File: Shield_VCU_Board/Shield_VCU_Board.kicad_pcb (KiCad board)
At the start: 2 copper layers, 250.5 x 107.1 mm, 148 parts, among them J1 Conn_02x08_Odd_Even, J10 Main_Supply, J11 Conn_01x40_Socket, J13 Conn_Molex_TouchPanel, J14 CAN_OUT, J15 Conn_01x04_Socket, J2 Conn_02x10_Odd_Even, J3/1 NXP3, J4 Conn_02x08_Odd_Even, J5 Conn_02x10_Odd_Even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

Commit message: 7seg+LED changes
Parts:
- added Q1: BFR92, Package_TO_SOT_SMD:SOT-323_SC-70, B.Cu at (258.2, 62.8)
- added Q2: BFR92, Package_TO_SOT_SMD:SOT-323_SC-70, B.Cu at (258.2, 73.8)
- added Q3: BFR92, Package_TO_SOT_SMD:SOT-323_SC-70, B.Cu at (258.2, 84.7)
- added Q4: BFR92, Package_TO_SOT_SMD:SOT-323_SC-70, B.Cu at (258.2, 95.8)
- added R1: 1k, Resistor_SMD:R_1206_3216Metric_Pad1.30x1.75mm_HandSolder, B.Cu at (257.6, 59.3)
- added R17: 1k, Resistor_SMD:R_1206_3216Metric_Pad1.30x1.75mm_HandSolder, B.Cu at (257.6, 69.9)
- added R18: 1k, Resistor_SMD:R_1206_3216Metric_Pad1.30x1.75mm_HandSolder, B.Cu at (257.6, 80.6)
- added R23: 1k, Resistor_SMD:R_1206_3216Metric_Pad1.30x1.75mm_HandSolder, B.Cu at (257.6, 91.2)
- moved C36 30.1 mm to (107.3, 84.8), turned to 180 degrees
- moved PD1 4.46 mm to (163.5, 75.2)
- moved R20 2.64 mm to (178.4, 72.1)
- moved INT1 2.56 mm to (162.6, 72.1)
- moved CS1 2.42 mm to (162.3, 68.9)
- moved R21 2.24 mm to (178.3, 74.4)
- moved MOSI1 1.10 mm to (153.7, 66.0)
- moved MISO1 0.71 mm to (151.5, 65.0)
- moved SCK1 0.30 mm to (149.3, 63.7)
- turned C35 to 90 degrees
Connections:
- net Net-(U1-DIG0) renamed /7U8
- net Net-(U1-DIG1) renamed /7U5
- net Net-(U1-DIG2) renamed /7U2
- net Net-(U1-DIG3) renamed /7U7
- net Net-(U1-DIG4) renamed /7U1
- net Net-(U1-DIG5) renamed /7U4
- net Net-(U1-DIG6) renamed /7U6
- net Net-(U1-DIG7) renamed /7U3
- J2 pad 1: MC_INT -> MC_PD
- J2 pad 15: unconnected-(J2-Pin_15-Pad15) -> AUD_SHDN
- J2 pad 2: AUD_SHDN -> unconnected-(J2-Pin_2-Pad2)
- J2 pad 3: MC_PD -> MC_INT
- R2 pad 1: LED1_PTB9 -> Net-(Q1-E)
- R3 pad 1: LED2_PTA12 -> Net-(Q2-E)
- R4 pad 1: LED3_PTA24 -> Net-(Q3-E)
- R5 pad 1: LED4_PTA25 -> Net-(Q4-E)
- U3 pad 10: FT_PD -> FT_INT
- U3 pad 11: MC_PD -> MC_INT
- U3 pad 8: MC_INT -> MC_PD
- U3 pad 9: FT_INT -> FT_PD
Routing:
- net +12V: track 343.1 -> 500.2 mm
- net LED4_PTA25: track 2.40 -> 34.9 mm
- net LED3_PTA24: track 2.88 -> 24.9 mm
- net LED1_PTB9: track 3.06 -> 20.5 mm
- net LED2_PTA12: track 2.49 -> 19.9 mm
- net AUD_SHDN: track 107.2 -> 94.2 mm
- net FT_INT: track 84.8 -> 79.3 mm, vias 2 -> 0
- net Net-(Q4-E): track 0.00 -> 5.00 mm
- net Net-(Q2-E): track 0.00 -> 4.89 mm
- net Net-(Q3-E): track 0.00 -> 4.77 mm
- net Net-(Q1-E): track 0.00 -> 4.77 mm
- net Net-(Q4-B): track 0.00 -> 3.90 mm
- net Net-(Q3-B): track 0.00 -> 3.43 mm
- net FT_PD: track 75.8 -> 79.2 mm
- net 3V3_DSPL: track 191.9 -> 188.5 mm
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
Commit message: All_wires_to_0.2mm
All the wires had the size forced to 0.2mm
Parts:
- removed F1: Fuse_3A, Fuse:Fuseholder_Blade_Mini_Keystone_3568
- RN8: value R_Pack_33R_04 -> 33R
- moved J10 18.4 mm to (48.0, 56.7), turned to 90 degrees
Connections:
- J10 pad 2: Net-(J10-Pin_2) -> +12V
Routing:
- net GND: track 277.1 -> 437.3 mm, vias 21 -> 26
- net LED4_PTA25: track 34.9 -> 76.9 mm
- net LED3_PTA24: track 24.9 -> 66.9 mm
- net LED2_PTA12: track 19.9 -> 61.9 mm
- net LED1_PTB9: track 20.5 -> 62.5 mm
- net Net-(J10-Pin_2): track 26.1 -> 0.00 mm
- net AUD_SHDN: track 94.2 -> 90.7 mm
- net Net-(7U1-G): track 156.6 -> 158.5 mm
- net Net-(7U1-B): track 165.0 -> 166.6 mm
- net Net-(7U1-F): track 159.1 -> 160.5 mm
- net 7S_NXP_SCL: track 235.3 -> 234.5 mm
- net 5V_BKLT: track 33.2 -> 32.6 mm
- net LED_A: track 19.8 -> 19.2 mm

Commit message: Wires sized
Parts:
- added NT1: NetTie_2, NetTie:NetTie-2_SMD_Pad2.0mm, F.Cu at (140.9, 47.7)
- moved C10 1.66 mm to (81.0, 76.6)
- moved C11 1.66 mm to (83.2, 76.6)
- moved C9 1.66 mm to (78.8, 76.6)
- moved AUDV3.3 0.61 mm to (77.4, 92.1)
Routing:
- net GND: track 437.3 -> 447.7 mm, vias 26 -> 27
- net Net-(RN8-R3.2): track 55.5 -> 60.1 mm
- net 3V3_DSPL: track 188.5 -> 186.2 mm
- net Net-(RN8-R4.2): track 53.0 -> 54.3 mm
- net 3V3_SPKR: track 37.0 -> 38.4 mm
- net Net-(C3-Pad1): track 5.52 -> 6.64 mm
- net GNDA: track 53.3 -> 54.2 mm
- net 5V_BKLT: track 32.6 -> 31.7 mm
- net Net-(D14-A): track 3.51 -> 4.22 mm
- net BL_PWM: track 54.8 -> 55.4 mm
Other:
- board text added: "1.Change wires width depending on current consumption 2.Connect all required vias for GND planes"

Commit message: LED supply wires correction
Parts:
- moved R17 1.10 mm to (256.6, 70.5)
- moved R1 1.02 mm to (256.6, 59.7)
- moved R18 1.01 mm to (256.6, 80.2)
- moved R23 0.98 mm to (256.6, 91.5)
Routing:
- net +12V: track 500.5 -> 457.3 mm
- net GND: track 447.7 -> 460.0 mm
- net LED1_PTB9: track 62.5 -> 54.3 mm, vias 1 -> 0
- net LED2_PTA12: track 61.9 -> 54.8 mm, vias 1 -> 0
- net LED4_PTA25: track 76.9 -> 71.7 mm, vias 1 -> 0
- net LED3_PTA24: track 66.9 -> 62.2 mm, vias 1 -> 0
- net Net-(J2-Pin_12): track 1.54 -> 0.39 mm
- net /7U2: track 60.8 -> 61.6 mm
- net Net-(Q3-B): track 3.43 -> 4.20 mm
- net Net-(7U1-A): track 166.0 -> 165.4 mm
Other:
- board text removed: "1.Change wires width depending on current consumption 2.Connect all required vias for GND planes"

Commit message: GND empty spot extension
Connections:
- J2 pad 10: LED1_PTB9 -> unconnected-(J2-Pin_10-Pad10)
- J2 pad 4: LED2_PTA12 -> unconnected-(J2-Pin_4-Pad4)
- J2 pad 6: LED3_PTA24 -> unconnected-(J2-Pin_6-Pad6)
- J2 pad 8: LED4_PTA25 -> unconnected-(J2-Pin_8-Pad8)
- J6 pad 11: unconnected-(J6-Pin_11-Pad11) -> LED3_PTA24
- J6 pad 13: unconnected-(J6-Pin_13-Pad13) -> LED4_PTA25
- J6 pad 7: unconnected-(J6-Pin_7-Pad7) -> LED1_PTB9
- J6 pad 9: unconnected-(J6-Pin_9-Pad9) -> LED2_PTA12
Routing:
- net LED1_PTB9: track 54.3 -> 31.9 mm
- net LED2_PTA12: track 54.8 -> 35.4 mm
- net LED3_PTA24: track 62.2 -> 45.7 mm
- net LED4_PTA25: track 71.7 -> 58.1 mm
- net +12V: track 457.3 -> 457.9 mm
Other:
- board text removed: "!!!GND planes NOT connected!!!"

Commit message: GND lines added + JST connector
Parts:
- J7: footprint Connector_PinSocket_2.00mm:PinSocket_2x01_P2.00mm_Vertical_SMD -> ALibrary:JST_PH_B2B-PH-K_1x02_P2.00mm_Vertical_GHST
- J8: footprint Connector_Molex:Molex_KK-396_A-41791-0002_1x02_P3.96mm_Vertical -> ALibrary:JST_PH_B2B-PH-K_1x02_P2.00mm_Vertical_GHST
- moved SCK1 14.2 mm to (163.5, 64.6)
- moved MISO1 12.1 mm to (163.5, 66.8)
- moved MOSI1 10.2 mm to (163.5, 68.9)
- moved J8 2.75 mm to (78.2, 70.7)
- moved CS1 2.49 mm to (163.5, 71.1)
- moved INT1 1.45 mm to (163.5, 73.2)
- moved NT1 0.90 mm to (140.9, 48.6)
- moved PD1 0.20 mm to (163.5, 75.4)
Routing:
- net GND: track 460.0 -> 808.7 mm, vias 27 -> 47
- net Net-(7U1-G): track 158.5 -> 167.3 mm
- net Net-(J8-Pin_1): track 14.0 -> 11.3 mm
- net FT_MOSI: track 84.2 -> 86.6 mm
- net Net-(RN8-R3.2): track 60.1 -> 57.9 mm
- net /7U3: track 47.1 -> 44.9 mm
- net 3V3_DSPL: track 186.2 -> 188.3 mm
- net FT_T_SCK: track 83.9 -> 86.0 mm
- net FT_MISO: track 83.1 -> 85.0 mm
- net Net-(J8-Pin_2): track 20.7 -> 18.8 mm
- net /7U6: track 26.0 -> 24.2 mm
- net Net-(7U1-A): track 165.4 -> 163.7 mm
- net /7U2: track 61.6 -> 60.8 mm
- net FT_CS: track 81.0 -> 81.6 mm
- net FT_INT: track 79.3 -> 79.8 mm

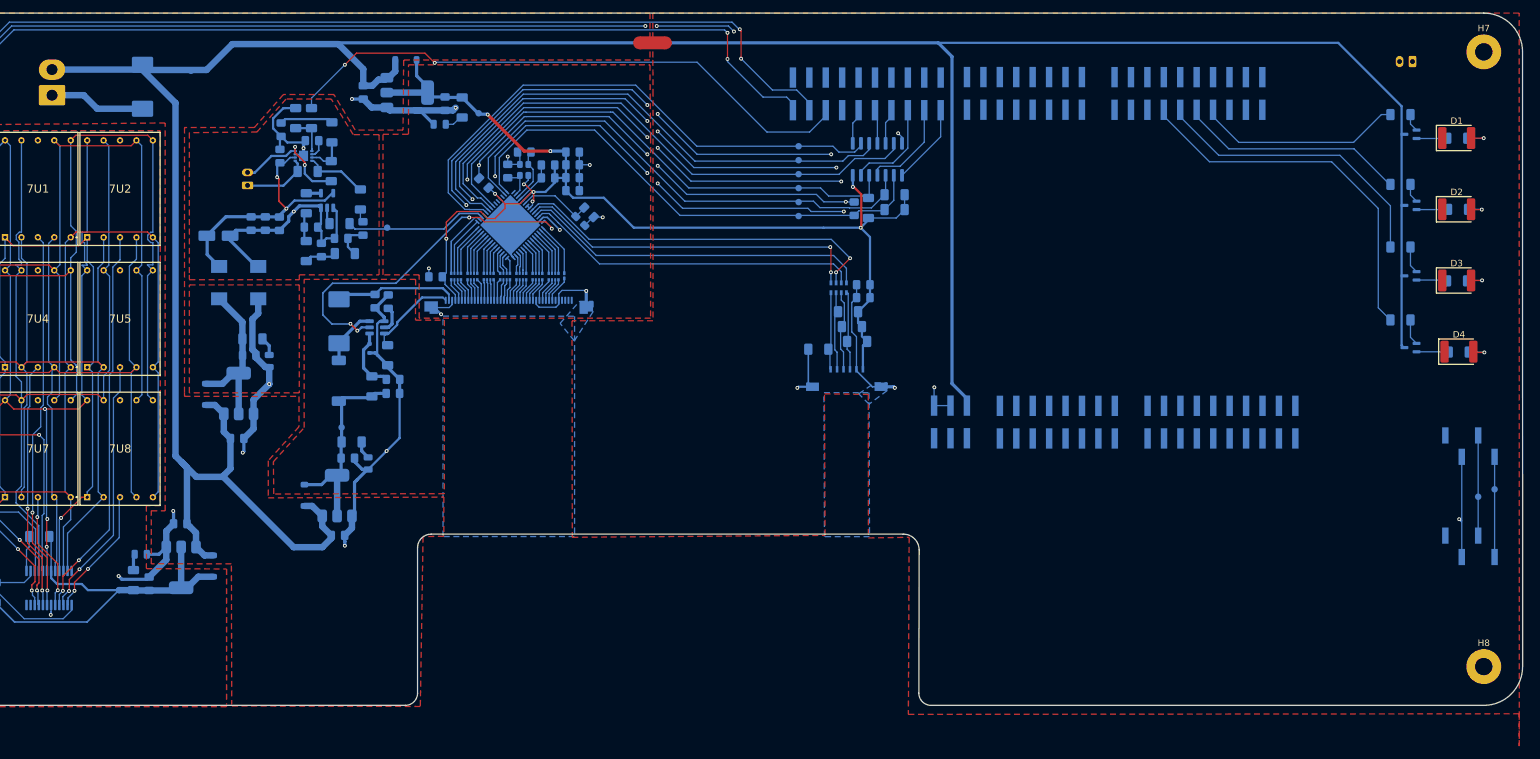
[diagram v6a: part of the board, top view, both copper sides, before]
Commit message: JST connectors added
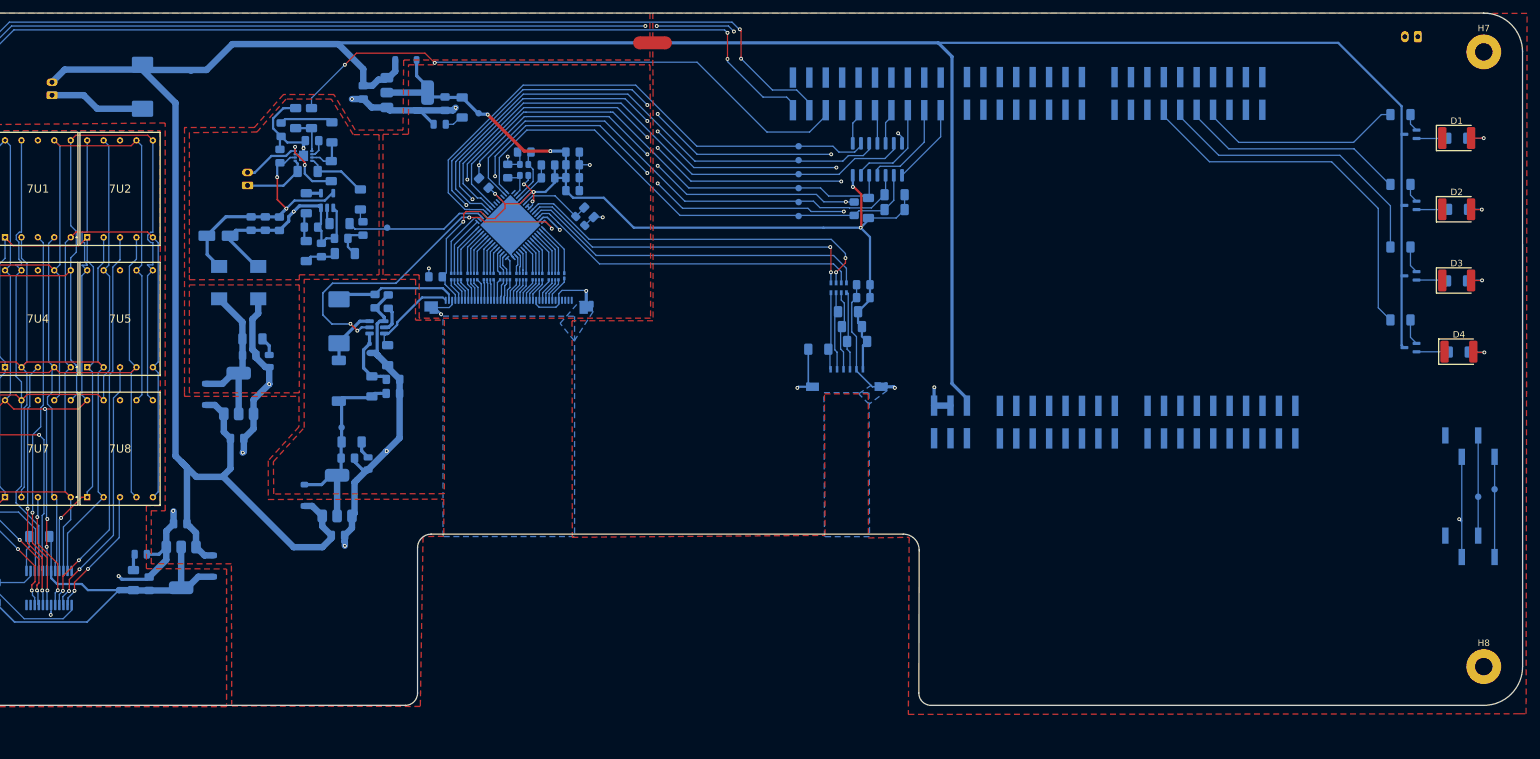
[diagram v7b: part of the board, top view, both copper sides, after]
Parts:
- J10: footprint Connector_Molex:Molex_KK-396_A-41791-0002_1x02_P3.96mm_Vertical -> ALibrary:JST_PH_B2B-PH-K_1x02_P2.00mm_Vertical_GHST
- NT1: value NetTie_2 -> 12VTie
- moved J7 3.94 mm to (259.3, 47.6)
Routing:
- net 3V3_DSPL: track 188.3 -> 187.5 mm
- net +12V: track 457.9 -> 458.7 mm
- net Net-(RN8-R3.2): track 57.9 -> 57.3 mm

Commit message: JST CAN connector change
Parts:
- J14: footprint Connector_PinHeader_2.54mm:PinHeader_1x04_P2.54mm_Vertical_SMD_Pin1Left -> ALibrary:JST_PH_B2B-PH-K_1x02_P2.00mm_Vertical_GHST
- moved J14 1.37 mm to (267.8, 125.2), turned to 0 degrees
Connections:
- CAN_H1 pad 1: Net-(J14-Pin_1) -> Net-(J14-Pin_2)
- CAN_L1 pad 1: Net-(J14-Pin_2) -> Net-(J14-Pin_1)
- J15 pad 1: Net-(J14-Pin_1) -> Net-(J14-Pin_2)
- J15 pad 2: Net-(J14-Pin_2) -> Net-(J14-Pin_1)
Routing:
- net GND: track 808.5 -> 794.6 mm
- net Net-(J14-Pin_2): track 15.5 -> 13.1 mm
- net Net-(J14-Pin_1): track 15.5 -> 16.2 mm
